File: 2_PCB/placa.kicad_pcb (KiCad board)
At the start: 2 copper layers, 38.1 x 95.2 mm, 41 parts, among them J1 Screw_Terminal_01x02, J2 Conn_01x05_Male, J3 Screw_Terminal_01x02, J4 TestPoints, SW1 SW_Push, U1 STM32L051C8Tx, U2 Ai-Thinker-Ra-01, Y1 8 MHz, Y2 32.768 kHz

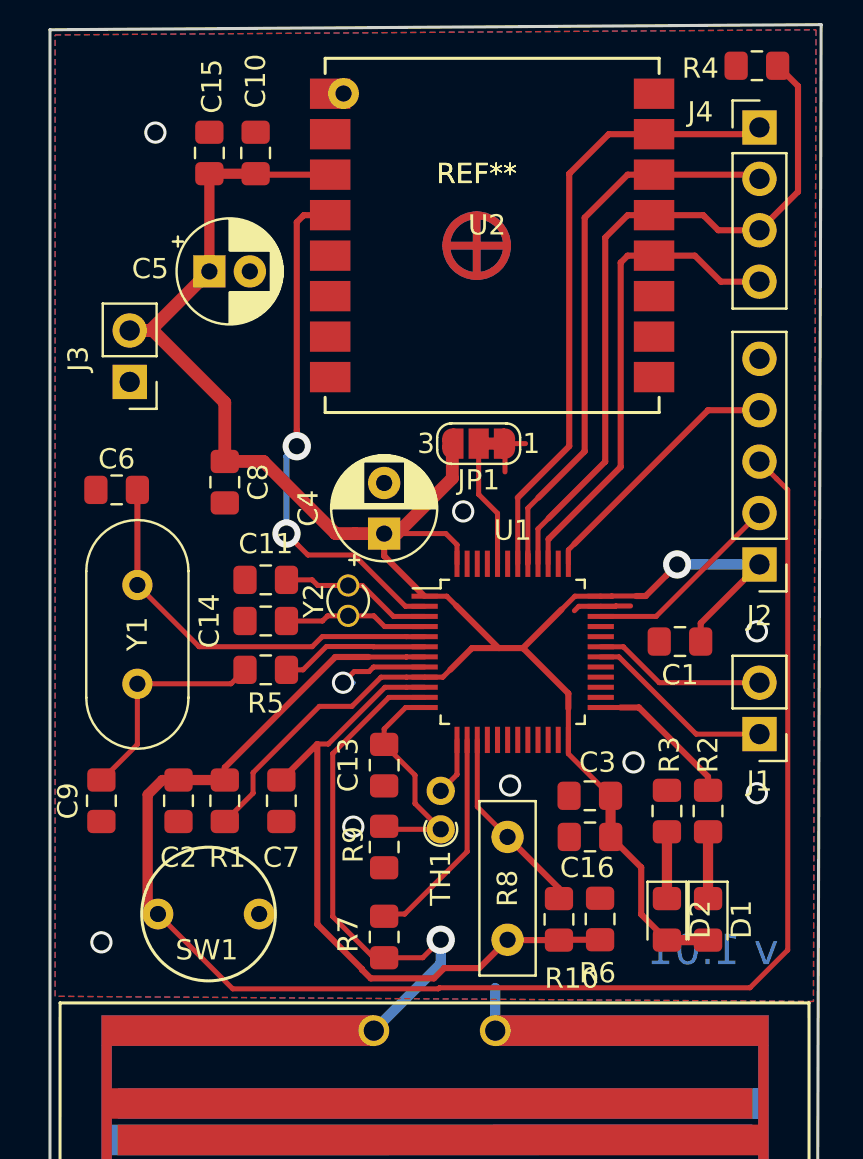
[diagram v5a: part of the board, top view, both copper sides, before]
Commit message: PCB version 1.1: Easier to home etch and added a BOOT0 PD resistor
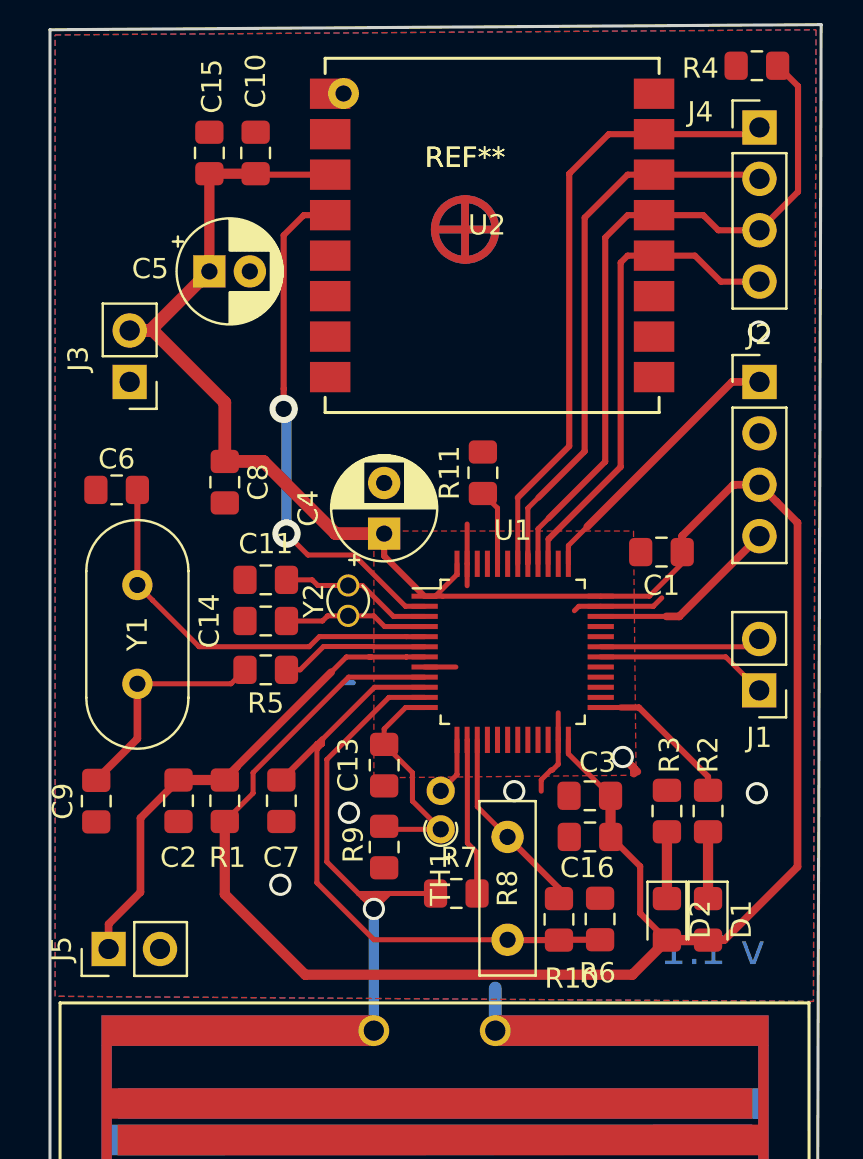
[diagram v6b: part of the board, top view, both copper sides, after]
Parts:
- removed JP1: SolderJumper_3_Bridged12, Jumper:SolderJumper-3_P1.3mm_Bridged12_RoundedPad1.0x1.5mm_NumberLabels
- removed SW1: SW_Push, TCC:BUTTON_5mm
- added J5: Conn_01x02_Male, Connector_PinHeader_2.54mm:PinHeader_1x02_P2.54mm_Vertical, F.Cu at (106.5, 72.8)
- added R11: 10k, Resistor_SMD:R_0805_2012Metric_Pad1.15x1.40mm_HandSolder, F.Cu at (125.0, 49.3)
- J2: value Conn_01x05_Male -> Conn_01x04_Male; footprint Connector_PinHeader_2.54mm:PinHeader_1x05_P2.54mm_Vertical -> Connector_PinHeader_2.54mm:PinHeader_1x04_P2.54mm_Vertical
- moved J2 9.02 mm to (138.7, 44.8), turned to 0 degrees
- moved C1 4.51 mm to (133.8, 53.2)
- moved R7 4.16 mm to (123.7, 70.1), turned to 0 degrees
- moved J1 2.16 mm to (138.7, 60.1)
- moved REF** 0.98 mm to (124.1, 37.3) (x2)
- moved C9 0.25 mm to (105.9, 65.5)
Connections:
- J2 pad 1: VCC -> /SWCLK
- J2 pad 2: /SWDIO -> GND
- J2 pad 3: /NRST -> VCC
- J2 pad 4: /SWCLK -> /SWDIO
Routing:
- net /NRST: track 81.1 -> 25.7 mm
- net VCC: track 110.7 -> 141.2 mm, vias 1 -> 0
- net GND: track 12.3 -> 18.1 mm, vias 9 -> 6
- net /PWR_MS: track 10.6 -> 7.79 mm
- net Net-(R11-Pad1): track 6.32 -> 3.77 mm
- net /ADC_RH: track 33.8 -> 31.6 mm
- net /ADC_MS: track 26.4 -> 27.4 mm
- net /UART_TX: track 9.42 -> 8.51 mm
- net /SWCLK: track 13.0 -> 13.7 mm
- net /UART_RX: track 8.58 -> 7.99 mm
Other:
- board text added: "v 1.1"
- board text removed: "v 1.01"

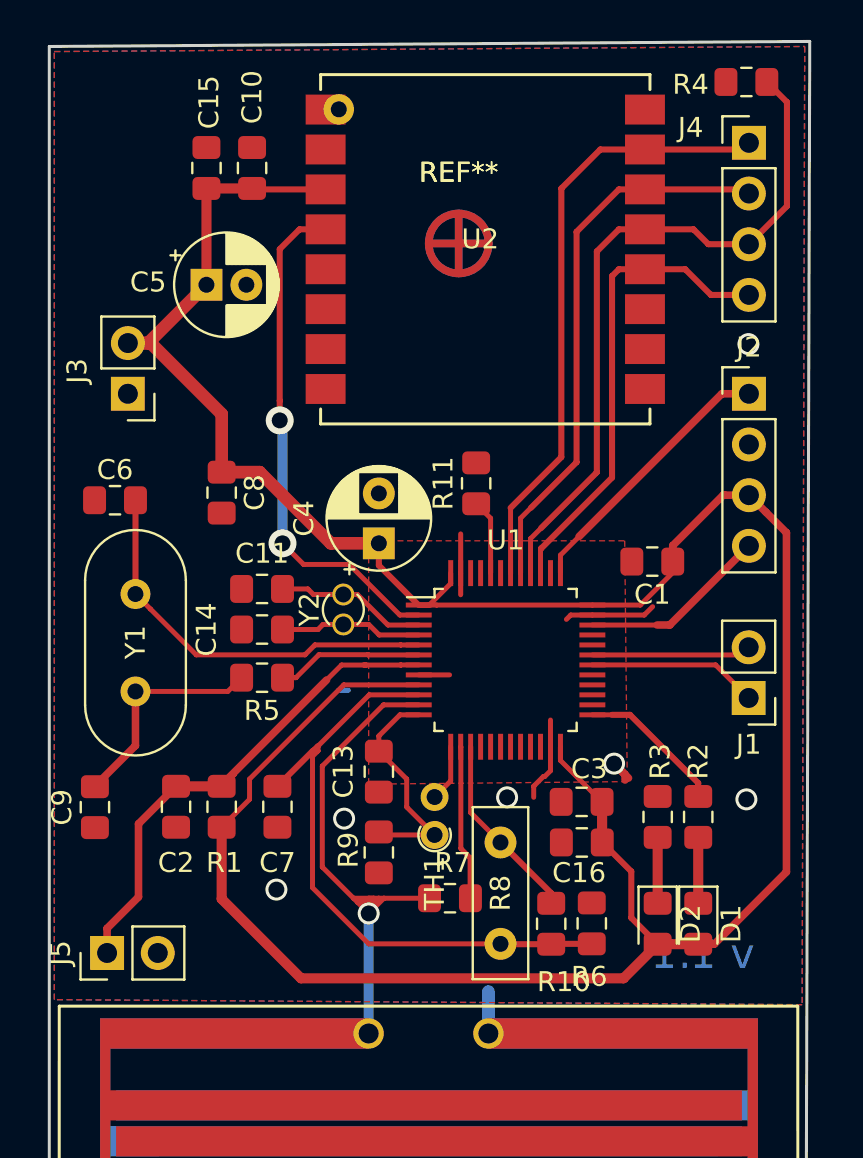
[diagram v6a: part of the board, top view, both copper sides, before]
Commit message: New branch for new HW revision. To add different layout, comparator for MS, change in RH circ
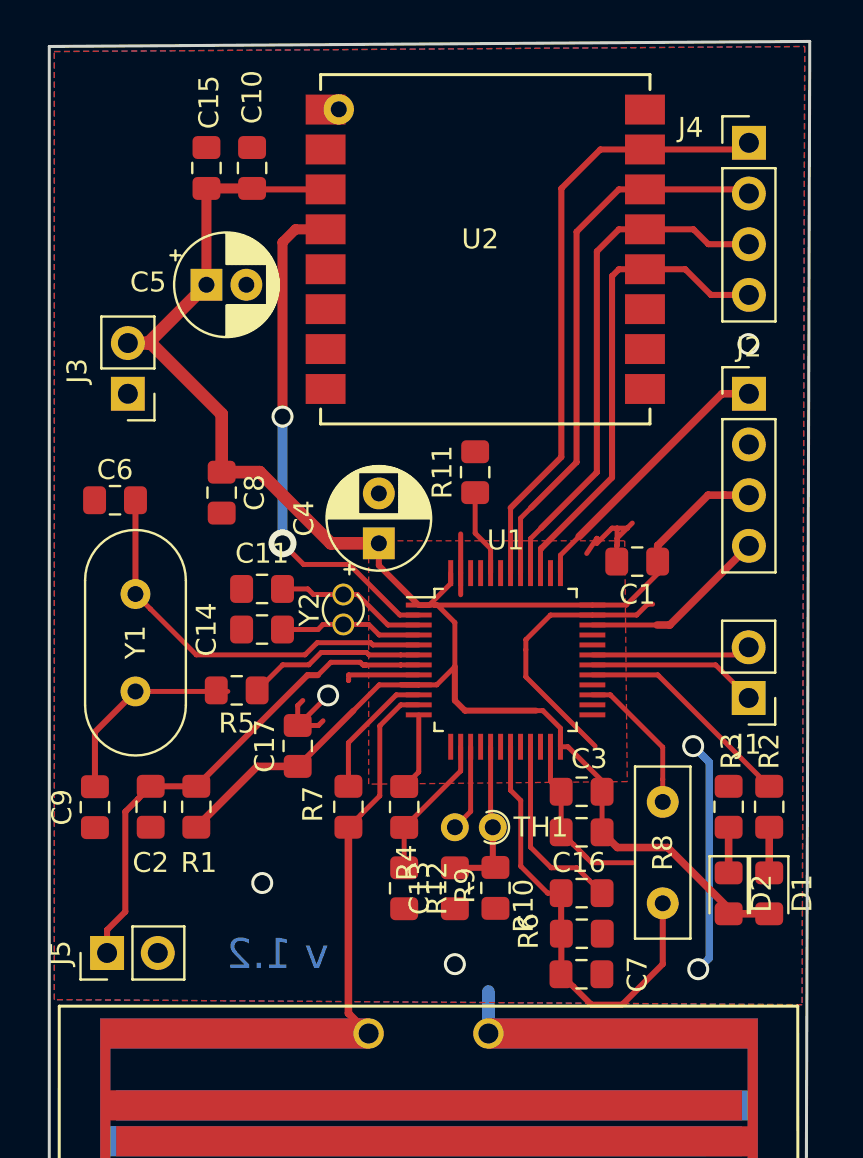
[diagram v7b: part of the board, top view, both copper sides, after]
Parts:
- removed REF**: Fiducial_classic_Small_CopperBottom_Type1, Fiducial:Fiducial_classic_Small_CopperBottom_Type1
- removed REF**: Fiducial_classic_Small_CopperTop_Type1, Fiducial:Fiducial_classic_Small_CopperTop_Type1
- added C17: 100n, Capacitor_SMD:C_0805_2012Metric_Pad1.15x1.40mm_HandSolder, F.Cu at (116.1, 62.5)
- added R12: 22k, Resistor_SMD:R_0805_2012Metric_Pad1.15x1.40mm_HandSolder, F.Cu at (121.4, 69.6)
- C13, C7: value 660n -> 10n
- R10, R6: value 180k -> 47k
- R4: value 100k -> 22k
- moved R4 40.2 mm to (121.4, 65.5), turned to 270 degrees
- moved C7 17.4 mm to (130.3, 73.9), turned to 0 degrees
- moved R8 8.38 mm to (134.4, 65.3)
- moved C13 6.97 mm to (124.0, 69.6)
- moved R7 6.85 mm to (118.6, 65.5), turned to 90 degrees
- moved R9 6.11 mm to (126.0, 69.6)
- moved D2 3.87 mm to (137.7, 69.9)
- moved D1 3.87 mm to (139.7, 69.9)
- moved R3 3.59 mm to (137.7, 65.5)
- moved R2 3.59 mm to (139.7, 65.5)
- moved TH1 2.94 mm to (125.9, 66.5), turned to 180 degrees
- moved R10 2.16 mm to (130.3, 69.8), turned to 180 degrees
- moved R5 1.42 mm to (113.0, 59.7)
- moved C2 1.27 mm to (108.7, 65.5)
- moved R1 1.27 mm to (111.0, 65.5)
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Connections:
- net /ADC_MS renamed /COMP_P
- R10 pad 1: /PWR_RH -> /PWR_RH_COMP
- R4 pad 1: /SPI_MISO -> /PWR_MS_COMP
- R4 pad 2: GND -> /COMP_M
- U1 pad 10: /ADC_RH -> /PWR_MS
- U1 pad 12: /ADC_TEMP -> /PWR_MS_COMP
- U1 pad 13: /PWR_TEMP -> Net-(U1-Pad13)
- U1 pad 14: /PWR_MS -> /COMP_M
- U1 pad 15: /PWR_RH -> /PWR_TEMP
- U1 pad 16: (no net) -> Net-(U1-Pad16)
- U1 pad 17: (no net) -> /ADC_TEMP
- U1 pad 18: (no net) -> Net-(U1-Pad18)
- U1 pad 19: (no net) -> /ADC_RH
- U1 pad 20: (no net) -> Net-(U1-Pad20)
- U1 pad 21: (no net) -> /PWR_RH_COMP
- U1 pad 22: (no net) -> Net-(U1-Pad22)
- U1 pad 25: /userLED -> Net-(U1-Pad25)
- U1 pad 26: (no net) -> Net-(U1-Pad26)
- U1 pad 27: (no net) -> /PWR_RH
- U1 pad 28: (no net) -> Net-(U1-Pad28)
- U1 pad 29: (no net) -> /userLED
- U1 pad 32: (no net) -> Net-(U1-Pad32)
- U1 pad 33: (no net) -> Net-(U1-Pad33)
- U1 pad 38: (no net) -> Net-(U1-Pad38)
- U1 pad 43: (no net) -> Net-(U1-Pad43)
- U1 pad 45: (no net) -> Net-(U1-Pad45)
- U1 pad 46: (no net) -> Net-(U1-Pad46)
- U2 pad 10: (no net) -> Net-(U2-Pad10)
- U2 pad 11: (no net) -> Net-(U2-Pad11)
- U2 pad 5: (no net) -> Net-(U2-Pad5)
- U2 pad 6: (no net) -> Net-(U2-Pad6)
- U2 pad 7: (no net) -> Net-(U2-Pad7)
- U2 pad 8: (no net) -> Net-(U2-Pad8)
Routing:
- net GND: track 18.1 -> 56.1 mm
- net VCC: track 141.2 -> 105.9 mm
- net /PWR_RH_COMP: track 0.00 -> 9.57 mm
- net /SPI_MISO: track 35.2 -> 25.9 mm
- net /ADC_RH: track 31.6 -> 22.5 mm
- net /COMP_P: track 27.4 -> 18.9 mm, vias 1 -> 0
- net /COMP_M: track 0.00 -> 7.24 mm
- net /PWR_MS_COMP: track 0.00 -> 3.89 mm
- net /userLED: track 7.39 -> 11.2 mm
- net /ADC_TEMP: track 11.4 -> 8.19 mm
- net /PWR_RH: track 9.51 -> 7.35 mm
- net /RCC_OSC_OUT: track 7.31 -> 8.93 mm
- net /PWR_TEMP: track 2.85 -> 4.36 mm
- net /PWR_MS: track 7.79 -> 6.70 mm
- net Net-(D2-Pad1): track 3.30 -> 2.29 mm
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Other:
- board text added: "v 1.2"
- board text removed: "v 1.1"

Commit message: Adding new files
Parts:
- R8: footprint Resistor_THT:R_Box_L8.4mm_W2.5mm_P5.08mm -> Resistor_THT:R_Axial_DIN0204_L3.6mm_D1.6mm_P1.90mm_Vertical
- moved R7 4.23 mm to (117.5, 69.6)
- moved R8 1.02 mm to (134.4, 64.3)
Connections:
- U1 pad 13: Net-(U1-Pad13) -> (no net)
- U1 pad 16: Net-(U1-Pad16) -> (no net)
- U1 pad 18: Net-(U1-Pad18) -> (no net)
- U1 pad 20: Net-(U1-Pad20) -> (no net)
- U1 pad 22: Net-(U1-Pad22) -> (no net)
- U1 pad 25: Net-(U1-Pad25) -> (no net)
- U1 pad 26: Net-(U1-Pad26) -> (no net)
- U1 pad 28: Net-(U1-Pad28) -> (no net)
- U1 pad 32: Net-(U1-Pad32) -> (no net)
- U1 pad 33: Net-(U1-Pad33) -> (no net)
- U1 pad 38: Net-(U1-Pad38) -> (no net)
- U1 pad 43: Net-(U1-Pad43) -> (no net)
- U1 pad 45: Net-(U1-Pad45) -> (no net)
- U1 pad 46: Net-(U1-Pad46) -> (no net)
- U2 pad 10: Net-(U2-Pad10) -> (no net)
- U2 pad 11: Net-(U2-Pad11) -> (no net)
- U2 pad 5: Net-(U2-Pad5) -> (no net)
- U2 pad 6: Net-(U2-Pad6) -> (no net)
- U2 pad 7: Net-(U2-Pad7) -> (no net)
- U2 pad 8: Net-(U2-Pad8) -> (no net)
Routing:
- net VCC: track 105.9 -> 113.8 mm
- net /COMP_P: track 18.9 -> 25.5 mm
- net GND: track 56.1 -> 49.9 mm, vias 6 -> 8
- net /PWR_MS: track 6.70 -> 11.2 mm
- net /ADC_RH: track 22.5 -> 23.9 mm, vias 0 -> 1
- net /PWR_RH: track 7.35 -> 6.22 mm
